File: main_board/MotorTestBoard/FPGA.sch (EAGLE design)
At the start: 32 parts, among them IC1 7805T, IC2 7805T, J5 XT-60BATT_LABEL, X3 22-23-2021, X4 332-14

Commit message: Update main board
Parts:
- removed C2, C9: 47uF, rcl:C-EUC1206
- removed U1: (no value), SparkFun-PowerIC:V_REG_LM1117SOT223
- removed X3: 22-23-2021, con-molex:22-23-2021
- removed X4: 332-14, con-garry:332-14
- added SV5: (no value), con-lstb:MA08-1
- added U$1: NODEMCU32S, nodeMCU:NODEMCU32S
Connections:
- removed net 3.3V: C9.1, U1.OUT, U1.OUT@1, X3-1.S
- removed net 5VI: C2.1, C5.1, IC2.VO, U1.IN
- removed net N$1: X4-1.S
- removed net N$10: X4-10.S
- removed net N$11: X4-8.S
- removed net N$12: X4-6.S
- removed net N$13: X4-4.S
- removed net N$14: X4-2.S
- removed net N$3: X4-5.S
- removed net N$4: X4-7.S
- removed net N$5: X4-9.S
- removed net N$6: X4-11.S
- removed net N$7: X4-13.S
- removed net N$8: X4-14.S
- removed net N$9: X4-12.S
- new net 5V1: C5.1, IC2.VO, U$1.5V
- new net CHARGE: JP2.16, SV5.1
- new net DONE: JP2.18, SV5.2
- new net ESP_EN: JP2.25, U$1.SEN
- new net ESP_RX: JP2.21, U$1.RX
- new net ESP_TX: JP2.23, U$1.TX
- new net IR1: JP2.24, SV5.7
- new net IR2: JP2.26, SV5.6
- new net IR3: JP2.15, SV5.5
- new net KICK: JP2.20, SV5.4
- new net KICK_CHIP: JP2.22, SV5.3
- net GND: now also JP1.1, JP1.39, JP2.2, JP2.40, SV5.8, U$1.GND, U$1.GND1, U$1.GND2, U$1.GND3; no longer C2.2, C9.2, U1.ADJ, X3-2.S
- net M11A: now also JP1.3
- net M11B: now also JP1.5
- net M12A: now also JP1.7
- net M12B: now also JP1.9
- net M13A: now also JP1.11
- net M13B: now also JP1.13
- net M1EA: now also JP1.4
- net M1EB: now also JP1.6
- net M1H1: now also JP1.8
- net M1H2: now also JP1.10
- net M1H3: now also JP1.12
- net M21A: now also JP1.27
- net M21B: now also JP1.29
- net M22A: now also JP1.31
- net M22B: now also JP1.33
- net M23A: now also JP1.35
- net M23B: now also JP1.37
- net M2EA: now also JP1.30
- net M2EB: now also JP1.32
- net M2H1: now also JP1.34
- net M2H2: now also JP1.36
- net M2H3: now also JP1.38
- net M31A: now also JP2.4
- net M31B: now also JP2.6
- net M32A: now also JP2.8
- net M32B: now also JP2.10
- net M33A: now also JP2.12
- net M33B: now also JP2.14
- net M3EA: now also JP2.3
- net M3EB: now also JP2.5
- net M3H1: now also JP2.7
- net M3H2: now also JP2.9
- net M3H3: now also JP2.11
- net M41A: now also JP2.28
- net M41B: now also JP2.30
- net M42A: now also JP2.32
- net M42B: now also JP2.34
- net M43A: now also JP2.36
- net M43B: now also JP2.38
- net M4EA: now also JP2.29
- net M4EB: now also JP2.31
- net M4H1: now also JP2.33
- net M4H2: now also JP2.35
- net M4H3: now also JP2.37
- net N$2: now also U$1.P22; no longer X4-3.S
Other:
- note removed: "POWER SUPPLY 3.3V"

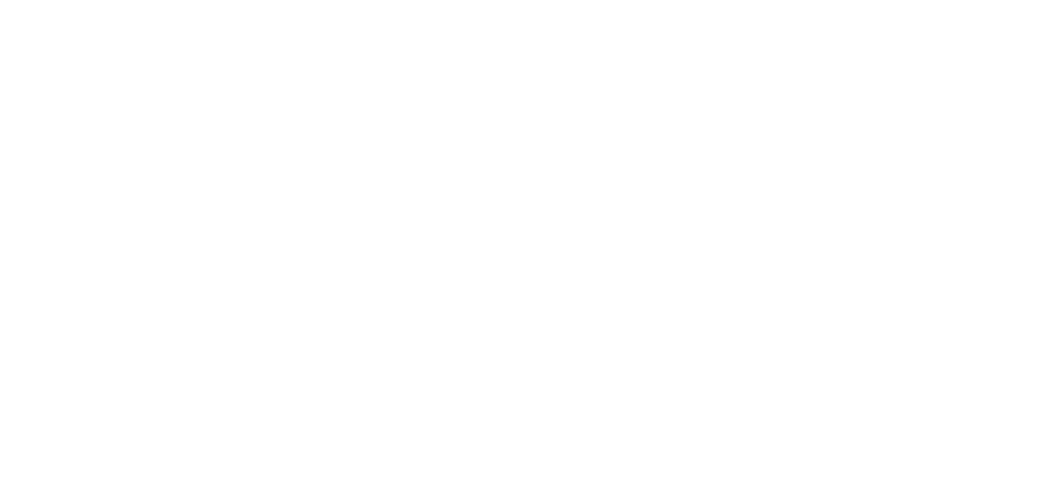
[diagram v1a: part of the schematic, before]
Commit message: New Dimensions for Main CKT
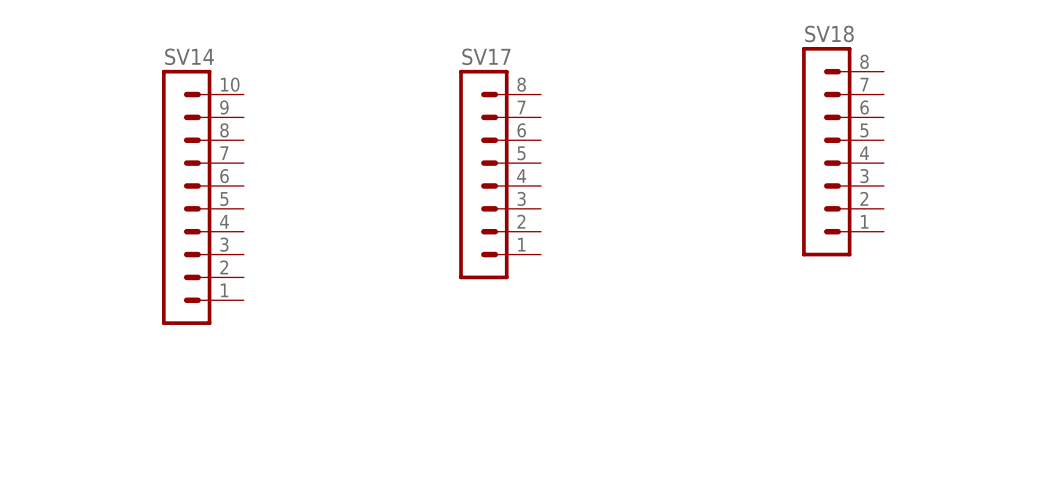
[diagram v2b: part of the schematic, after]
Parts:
- added SV14: (no value), con-lstb:MA10-1
- added SV17, SV18: (no value), con-lstb:MA08-1
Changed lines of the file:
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@@
 <setting verticaltext="up"/>
 </settings>
-<grid distance="0.1" unitdist="inch" unit="inch" style="lines" multiple="1" display="no" altdistance="0.1" altunitdist="inch" altunit="inch"/>
+<grid distance="0.1" unitdist="inch" unit="inch" style="lines" multiple="1" display="no" altdistance="0.01" altunitdist="inch" altunit="inch"/>
 <layers>
 <layer number="1" name="Top" color="4" fill="1" visible="no" active="no"/>
@@
 <part name="GND2" library="SparkFun" deviceset="GND" device=""/>
 <part name="SV5" library="con-lstb" deviceset="MA08-1" device=""/>
+<part name="SV14" library="con-lstb" deviceset="MA10-1" device=""/>
+<part name="SV17" library="con-lstb" deviceset="MA08-1" device=""/>
+<part name="SV18" library="con-lstb" deviceset="MA08-1" device=""/>
 </parts>
 <sheets>
@@
 <instance part="GND2" gate="1" x="-47.16" y="-169.18" rot="MR0"/>
 <instance part="SV5" gate="1" x="220.98" y="35.56" rot="MR180"/>
+<instance part="SV14" gate="1" x="-78.74" y="127"/>
+<instance part="SV17" gate="1" x="-45.72" y="129.54"/>
+<instance part="SV18" gate="1" x="-7.62" y="132.08"/>
 </instances>
 <busses>

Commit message: Placements
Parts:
- added U$4: BUCK, BUCK:BUCK
- added U1, U2: (no value), LP38690DT-3.3:LP38690DT-3.3
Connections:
- new net 12V: C1.1, C4.1, IC1.VI, IC2.VI, SV14.10, SV14.9, U$4.VOUT
- new net MD1: SV17.6, SV17.7, SV18.8
- new net MD1A: JP1.15, SV14.8
- new net MD1B: JP1.17, SV14.7
- new net MD2: SV17.4, SV17.5, SV18.7
- new net MD2A: JP1.19, SV14.6
- new net MD2B: JP1.21, SV14.5
- new net MD3: SV17.2, SV17.3, SV18.6
- new net MD3A: JP1.23, SV14.4
- new net MD3B: JP1.25, SV14.3
- new net MDACS_OUT: SV17.8
- new net MDH1: JP1.16, SV18.3
- new net MDH2: JP1.18, SV18.2
- new net MDH3: JP1.20, SV18.1
- net 18V: now also U$4.VIN; no longer C1.1, C4.1, IC1.VI, IC2.VI
- net 5V: now also SV17.1, SV18.5; no longer SV11.1, SV15.1, SV7.1, SV9.1
- net 5V1: now also SV11.1, SV15.1, SV7.1, SV9.1
- net GND: now also SV14.1, SV14.2, SV18.4, U$4.GND, U$4.GNDO
- net INPUT: now also U1.A, U1.~A, U2.A, U2.~A
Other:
- moved on the sheet: J5, S2, SV14, SV17, SV18

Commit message: Sch Comp
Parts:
- removed S2: (no value), switch:A68-A31
- added LED1, LED2, LED3, LED4, LED5, LED6, LED7: (no value), led:LEDSMT1206
- added R1, R2, R3, R4, R5, R6, R7: (no value), resistor:R-EU_R1206
- added U$5: (no value), switch_DA10:SWITCH_DA10
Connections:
- removed net N$25: S2A.P, S2B.P, U3.K
- new net ESP_REC: R7.1, U$1.P35
- new net ESP_TRANS: R6.1, U$1.P34
- new net FPGA_REC: JP1.22, R5.1
- new net N$1: J5.+, U$5.P
- new net N$10: LED3.A, R3.2
- new net N$13: LED4.A, R4.2
- new net N$16: LED5.A, R5.2
- new net N$19: LED6.A, R6.2
- new net N$22: LED7.A, R7.2
- new net N$4: LED1.A, R1.2
- new net N$7: LED2.A, R2.2
- net 12V: now also R4.1
- net 18V: now also R3.1, U1.K, U2.K, U3.K; no longer S2A.S, S2B.S
- net 5V: now also R2.1
- net 5V1: now also R1.1
- net GND: now also LED1.C, LED2.C, LED3.C, LED4.C, LED5.C, LED6.C, LED7.C
- net INPUT: now also U$5.S; no longer J5.+
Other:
- moved on the sheet: C1, C3, C4, C5, IC1, IC2, J5

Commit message: Route Complete
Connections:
- net N$1 renamed SUPP
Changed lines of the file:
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@@
 </segment>
 </net>
-<net name="M11" class="0">
+<net name="M11" class="6">
 <segment>
 <pinref part="SV1" gate="1" pin="8"/>
@@
 </segment>
 </net>
-<net name="M13" class="0">
+<net name="M13" class="6">
 <segment>
 <pinref part="SV1" gate="1" pin="6"/>
@@
 </segment>
 </net>
-<net name="M21" class="0">
+<net name="M21" class="6">
 <segment>
 <pinref part="SV2" gate="1" pin="8"/>
@@
 </segment>
 </net>
-<net name="M22" class="0">
+<net name="M22" class="6">
 <segment>
 <pinref part="SV2" gate="1" pin="7"/>
@@
 </segment>
 </net>
-<net name="M23" class="0">
+<net name="M23" class="6">
 <segment>
 <pinref part="SV2" gate="1" pin="6"/>
@@
 </segment>
 </net>
-<net name="M41" class="0">
+<net name="M41" class="6">
 <segment>
 <pinref part="SV4" gate="1" pin="8"/>
@@
 </segment>
 </net>
-<net name="M42" class="0">
+<net name="M42" class="6">
 <segment>
 <pinref part="SV4" gate="1" pin="7"/>
@@
 </segment>
 </net>
-<net name="M43" class="0">
+<net name="M43" class="6">
 <segment>
 <pinref part="SV4" gate="1" pin="6"/>
@@
 </segment>
 </net>
-<net name="M12" class="0">
+<net name="M12" class="6">
 <segment>
 <pinref part="SV1" gate="1" pin="7"/>
@@
 </segment>
 </net>
-<net name="IR3" class="4">
+<net name="IR3" class="3">
 <segment>
 <pinref part="SV5" gate="1" pin="5"/>
@@
 </segment>
 </net>
-<net name="5V1" class="0">
+<net name="5V1" class="1">
 <segment>
 <pinref part="U$1" gate="G$1" pin="5V"/>
@@
 </segment>
 </net>
-<net name="MD1" class="0">
+<net name="MD1" class="6">
 <segment>
 <pinref part="SV17" gate="1" pin="7"/>
@@
 </segment>
 </net>
-<net name="MD2" class="0">
+<net name="MD2" class="6">
 <segment>
 <pinref part="SV17" gate="1" pin="5"/>
@@
 </segment>
 </net>
-<net name="MD3" class="0">
+<net name="MD3" class="6">
 <segment>
 <pinref part="SV17" gate="1" pin="3"/>
@@
 </segment>
 </net>
-<net name="12V" class="0">
+<net name="12V" class="2">
 <segment>
 <pinref part="U$4" gate="G$1" pin="VOUT"/>
@@
 </segment>
 </net>
-<net name="N$1" class="0">
+<net name="SUPP" class="5">
 <segment>
 <pinref part="J5" gate="G$1" pin="+"/>
